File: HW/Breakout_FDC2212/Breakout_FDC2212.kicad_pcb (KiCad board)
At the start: 2 copper layers, 26 x 18 mm, 21 parts, among them J1 SM04B-SRSS-TB, J2 Conn_01x02, J3 Conn_01x02, J4 Conn_01x06, U5 625L3C040M00000, U6 FDC2212

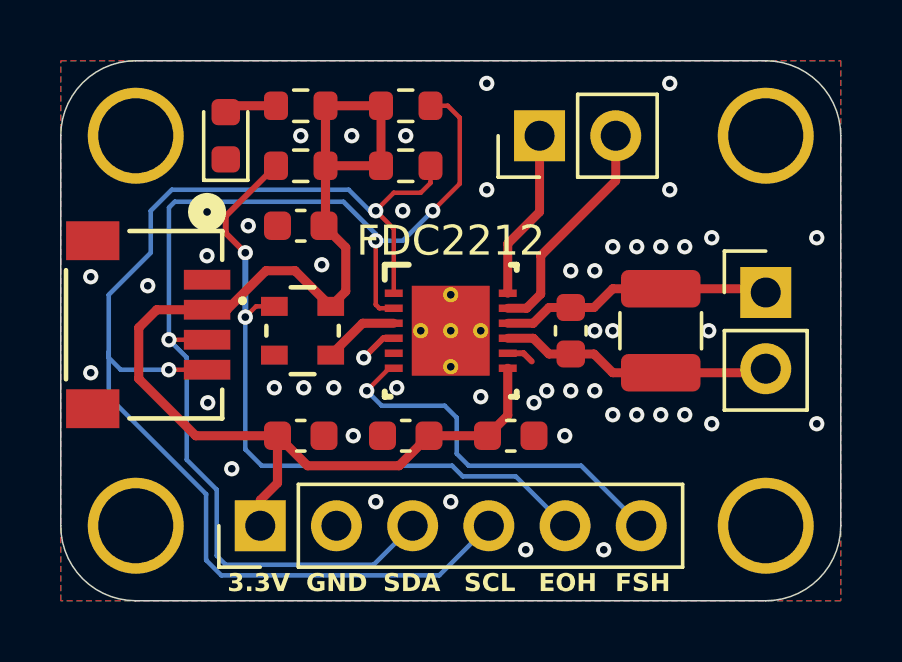
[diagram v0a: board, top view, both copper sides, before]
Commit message: Align pin holes for potential breadboard mounting
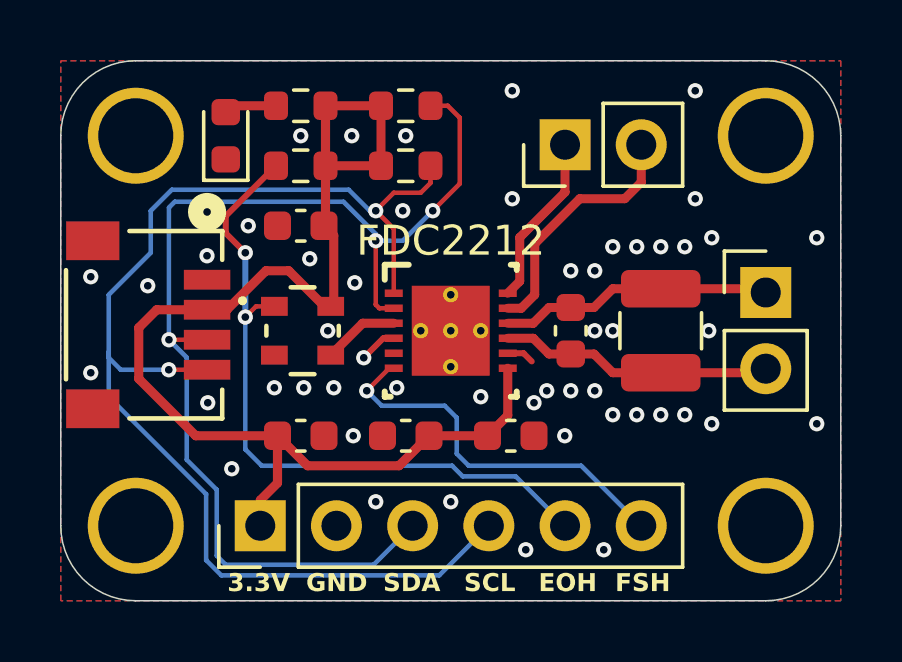
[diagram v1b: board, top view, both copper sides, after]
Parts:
- moved J3 0.90 mm to (116.8, 102.8)
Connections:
- net Net-(J3-Pin_1) renamed /SENSE1-
- net Net-(J3-Pin_2) renamed /SENSE1+
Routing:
- net /SENSE1+: track 7.61 -> 8.44 mm
- net GND: vias 49 -> 51
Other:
- board text added: "FDC2212 Breakout Capacitance-to-digital converter 28-bit resolution, L-C tank I2C address 0x2A Daniel Stiner 2025v0.2"
- board text removed: "FDC2212 Breakout Capacitance-to-digital converter 28-bit resolution, L-C tank I2C address 0x2A Daniel Stiner 2025v0.1"
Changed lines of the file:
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@@
 	(net 9 "/EOH")
 	(net 10 "unconnected-(U6-INTB-Pad5)")
-	(net 11 "Net-(J3-Pin_2)")
-	(net 12 "Net-(J3-Pin_1)")
+	(net 11 "/SENSE1+")
+	(net 12 "/SENSE1-")
 	(net 13 "/FDC_SHUTDOWN")
 	(footprint "FDC2212DNTT:DNT0012B"
@@
 			(size 0.249999 0.599999)
 			(layers "F.Cu" "F.Mask" "F.Paste")
-			(net 11 "Net-(J3-Pin_2)")
+			(net 11 "/SENSE1+")
 			(pinfunction "IN1A")
 			(pintype "input")
@@
 			(size 0.249999 0.599999)
 			(layers "F.Cu" "F.Mask" "F.Paste")
-			(net 12 "Net-(J3-Pin_1)")
+			(net 12 "/SENSE1-")
 			(pinfunction "IN1B")
 			(pintype "input")
@@
 	(footprint "Connector_PinHeader_2.54mm:PinHeader_1x02_P2.54mm_Vertical"
 		(layer "F.Cu")
-		(at 115.96 102.5 90)
+		(at 116.81 102.8 90)
 		(descr "Through hole straight pin header, 1x02, 2.54mm pitch, single row")
 		(tags "Through hole pin header THT 1x02 2.54mm single row")
@@
 			(layers "*.Cu" "*.Mask")
 			(remove_unused_layers no)
-			(net 12 "Net-(J3-Pin_1)")
+			(net 12 "/SENSE1-")
 			(pinfunction "Pin_1")
 			(pintype "passive")
@@
 			(layers "*.Cu" "*.Mask")
 			(remove_unused_layers no)
-			(net 11 "Net-(J3-Pin_2)")
+			(net 11 "/SENSE1+")
 			(pinfunction "Pin_2")
 			(pintype "passive")
@@
 		)
 	)
-	(gr_text "FDC2212 Breakout\nCapacitance-to-digital converter\n28-bit resolution, L-C tank\nI2C address 0x2A\n\nDaniel Stiner 2025v0.1"
+	(gr_text "FDC2212 Breakout\nCapacitance-to-digital converter\n28-bit resolution, L-C tank\nI2C address 0x2A\n\nDaniel Stiner 2025v0.2"
 		(at 121.5 114 0)
 		(layer "B.SilkS")
@@
 	)
 	(via
+		(at 109.8 107.4)
+		(size 0.508)
+		(drill 0.254)
+		(layers "F.Cu" "B.Cu")
+		(free yes)
+		(net 1)
+	)
+	(via
 		(at 118.4 106.2)
 		(size 0.508)
@@
 	)
 	(via
-		(at 108.7 106.8)
+		(at 108.3 106.6)
 		(size 0.508)
 		(drill 0.254)
@@
 	)
 	(via
-		(at 120.3 104.3)
-		(size 0.508)
-		(drill 0.254)
-		(layers "F.Cu" "B.Cu")
-		(free yes)
-		(net 1)
-	)
-	(via
-		(at 120.3 100.754)
+		(at 121.15 104.6)
 		(size 0.508)
 		(drill 0.254)
@@
 	)
 	(via
-		(at 114.2 100.754)
+		(at 115.05 101)
 		(size 0.508)
 		(drill 0.254)
@@
 	)
 	(via
+		(at 108.9 109)
+		(size 0.508)
+		(drill 0.254)
+		(layers "F.Cu" "B.Cu")
+		(free yes)
+		(net 1)
+	)
+	(via
 		(at 115.5 116.3)
 		(size 0.508)
@@
 	)
 	(via
-		(at 114.2 104.3)
+		(at 121.15 101)
+		(size 0.508)
+		(drill 0.254)
+		(layers "F.Cu" "B.Cu")
+		(free yes)
+		(net 1)
+	)
+	(via
+		(at 115.05 104.6)
 		(size 0.508)
 		(drill 0.254)
@@
 	)
 	(segment
-		(start 109 108.1875)
-		(end 109.5 107.6875)
+		(start 104.5 112.5)
+		(end 102.6 110.6)
 		(width 0.3048)
 		(layer "F.Cu")
@@
 	)
 	(segment
-		(start 104.875001 108.3)
-		(end 105.5391 108.3)
+		(start 108.7875 108.1875)
+		(end 109 108.1875)
+		(width 0.3048)
+		(layer "F.Cu")
+		(net 2)
+	)
+	(segment
+		(start 105.5391 108.3)
+		(end 106.8391 107)
 		(width 0.3048)
 		(layer "F.Cu")
@@
 	)
 	(segment
-		(start 105.5391 108.3)
-		(end 106.8391 107)
+		(start 103.2 108.3)
+		(end 105.5391 108.3)
+		(width 0.3048)
+		(layer "F.Cu")
+		(net 2)
+	)
+	(segment
+		(start 106.8391 107)
+		(end 107.6 107)
 		(width 0.3048)
 		(layer "F.Cu")
@@
 	)
 	(segment
-		(start 106.65 115.5)
-		(end 106.65 114.65)
+		(start 102.6 110.6)
+		(end 102.6 108.9)
 		(width 0.3048)
 		(layer "F.Cu")
@@
 	)
 	(segment
-		(start 109.5 106.225)
-		(end 108.775 105.5)
+		(start 106.65 115.5)
+		(end 106.65 114.65)
 		(width 0.3048)
 		(layer "F.Cu")
@@
 	)
 	(segment
-		(start 102.6 110.6)
-		(end 102.6 108.9)
-		(width 0.3048)
-		(layer "F.Cu")
-		(net 2)
-	)
-	(segment
 		(start 107.225 114.075)
 		(end 107.225 112.5)
@@
 	)
 	(segment
-		(start 107.8125 107)
-		(end 109 108.1875)
+		(start 109.1 105.825)
+		(end 108.775 105.5)
 		(width 0.3048)
 		(layer "F.Cu")
@@
 	)
 	(segment
-		(start 112.275 112.5)
-		(end 111.275 113.5)
-		(width 0.3048)
-		(layer "F.Cu")
-		(net 2)
-	)
-	(segment
-		(start 114.225 112.5)
-		(end 112.275 112.5)
+		(start 102.6 108.9)
+		(end 103.2 108.3)
 		(width 0.3048)
 		(layer "F.Cu")
@@
 	)
 	(segment
-		(start 102.6 108.9)
-		(end 103.2 108.3)
+		(start 112.275 112.5)
+		(end 111.275 113.5)
 		(width 0.3048)
 		(layer "F.Cu")
@@
 	)
 	(segment
-		(start 104.5 112.5)
-		(end 102.6 110.6)
+		(start 114.225 112.5)
+		(end 112.275 112.5)
 		(width 0.3048)
 		(layer "F.Cu")
@@
 	)
 	(segment
-		(start 103.2 108.3)
-		(end 104.875001 108.3)
+		(start 108.825 101.5)
+		(end 108.825 103.5)
 		(width 0.3048)
 		(layer "F.Cu")
@@
 	)
 	(segment
-		(start 108.825 101.5)
-		(end 108.825 103.5)
+		(start 107.6 107)
+		(end 108.7875 108.1875)
 		(width 0.3048)
 		(layer "F.Cu")
@@
 	)
 	(segment
-		(start 109.5 107.6875)
-		(end 109.5 106.225)
+		(start 107.225 112.5)
+		(end 104.5 112.5)
 		(width 0.3048)
 		(layer "F.Cu")
@@
 	)
 	(segment
-		(start 107.225 112.5)
-		(end 104.5 112.5)
+		(start 110.675 101.5)
+		(end 108.825 101.5)
 		(width 0.3048)
 		(layer "F.Cu")
@@
 	)
 	(segment
-		(start 110.675 101.5)
-		(end 108.825 101.5)
+		(start 109 108.1875)
+		(end 109.1 108.0875)
 		(width 0.3048)
 		(layer "F.Cu")
@@
 	)
 	(segment
-		(start 106.8391 107)
-		(end 107.8125 107)
+		(start 109.1 108.0875)
+		(end 109.1 105.825)
 		(width 0.3048)
 		(layer "F.Cu")
@@
 	)
 	(segment
-		(start 110.620602 108.249999)
-		(end 110.5 108.129397)
+		(start 112.9 101.5)
+		(end 112.325 101.5)
 		(width 0.1524)
 		(layer "F.Cu")
@@
 	)
 	(segment
-		(start 112.9 101.5)
-		(end 112.325 101.5)
+		(start 110.5 108.129397)
+		(end 110.620602 108.249999)
 		(width 0.1524)
 		(layer "F.Cu")
@@
 	)
 	(segment
-		(start 111.100001 108.249999)
-		(end 110.620602 108.249999)
+		(start 103.6064 109.299998)
+		(end 104.875001 109.299998)
 		(width 0.1524)
 		(layer "F.Cu")
@@
 	)
 	(segment
-		(start 103.6064 109.299998)
-		(end 104.875001 109.299998)
+		(start 110.620602 108.249999)
+		(end 111.100001 108.249999)
 		(width 0.1524)
 		(layer "F.Cu")
@@
 	)
 	(segment
-		(start 110.5 108.129397)
-		(end 110.5 106)
+		(start 110.5 106)
+		(end 110.5 108.129397)
 		(width 0.1524)
 		(layer "F.Cu")
@@
 	)
 	(segment
-		(start 116 107.776997)
-		(end 116 106.5)
+		(start 118.8 104.6)
+		(end 117.3 104.6)
+		(width 0.3)
+		(layer "F.Cu")
+		(net 11)
+	)
+	(segment
+		(start 117.3 104.6)
+		(end 115.8 106.1)
+		(width 0.3)
+		(layer "F.Cu")
+		(net 11)
+	)
+	(segment
+		(start 115.350001 108.249999)
+		(end 114.899999 108.249999)
 		(width 0.3)
 		(layer "F.Cu")
@@
 	)
 	(segment
-		(start 115.526998 108.249999)
-		(end 116 107.776997)
+		(start 115.8 107.8)
+		(end 115.350001 108.249999)
 		(width 0.3)
 		(layer "F.Cu")
@@
 	)
 	(segment
-		(start 114.899999 108.249999)
-		(end 115.526998 108.249999)
+		(start 115.8 106.1)
+		(end 115.8 107.8)
 		(width 0.3)
 		(layer "F.Cu")
@@
 	)
 	(segment
-		(start 116 106.5)
-		(end 118.5 104)
+		(start 119.35 102.8)
+		(end 119.35 104.05)
 		(width 0.3)
 		(layer "F.Cu")
@@
 	)
 	(segment
-		(start 118.5 104)
-		(end 118.5 102.5)
+		(start 119.35 104.05)
+		(end 118.8 104.6)
 		(width 0.3)
 		(layer "F.Cu")
@@
 	)
 	(segment
-		(start 114.899999 106.100001)
-		(end 114.899999 107.75)
+		(start 114.899999 107.75)
+		(end 115.3 107.349999)
+		(width 0.3)
+		(layer "F.Cu")
+		(net 12)
+	)
+	(segment
+		(start 116.81 104.38148)
+		(end 115.3 105.89148)
 		(width 0.3)
 		(layer "F.Cu")
@@
 	)
 	(segment
-		(start 115.96 102.5)
-		(end 115.96 105.04)
+		(start 115.3 105.89148)
+		(end 115.3 107.349999)
 		(width 0.3)
 		(layer "F.Cu")
@@
 	)
 	(segment
-		(start 115.96 105.04)
-		(end 114.899999 106.100001)
+		(start 116.81 102.8)
+		(end 116.81 104.38148)
 		(width 0.3)
 		(layer "F.Cu")
